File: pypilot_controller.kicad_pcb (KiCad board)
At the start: 4 copper layers, 76.6 x 50.6 mm, 82 parts, among them J1 power+, J2 power-, J3 power+, J4 power+, J5 UART_Device, J6 Rudder, J7 End Stops, J8 Conn_01x02, J9 ISP, Q1 Q_NMOS_GDS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

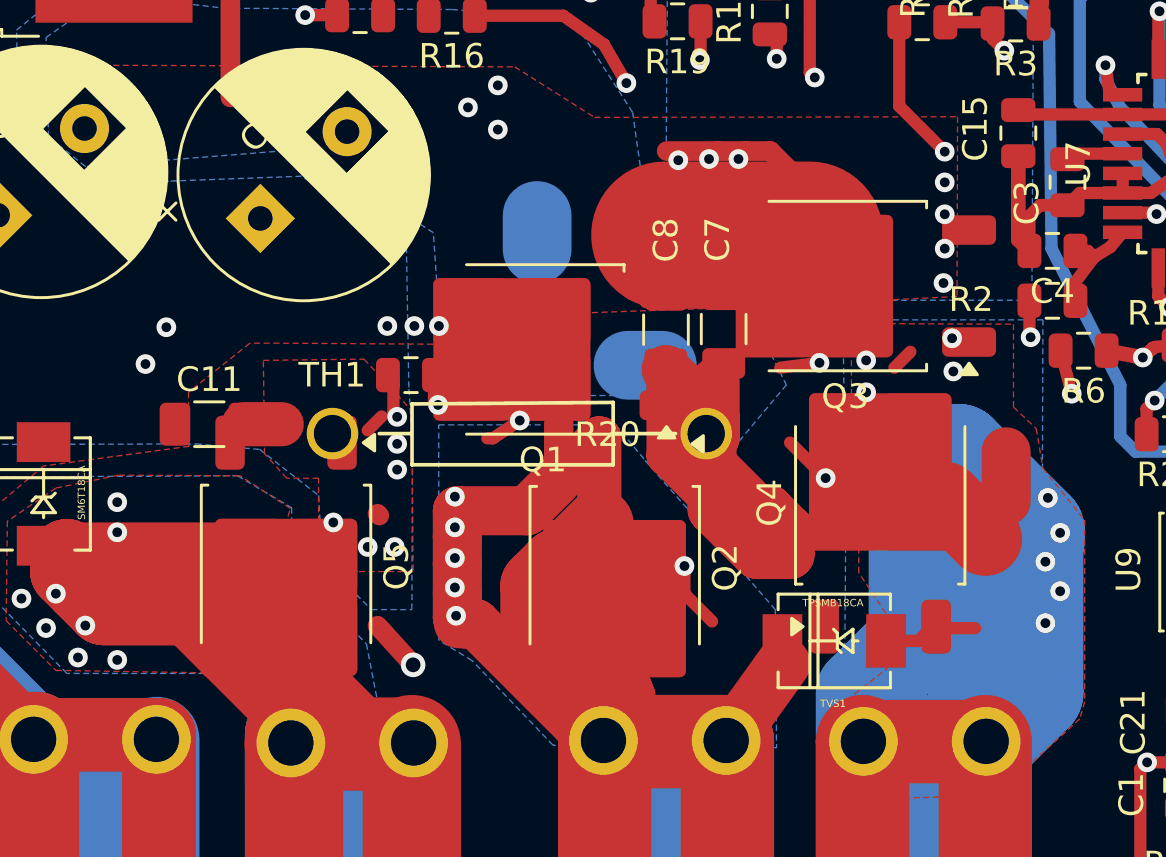
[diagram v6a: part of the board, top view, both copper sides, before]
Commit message: Shifted MOSFET locations to match original board
Centroid varies from original footprint
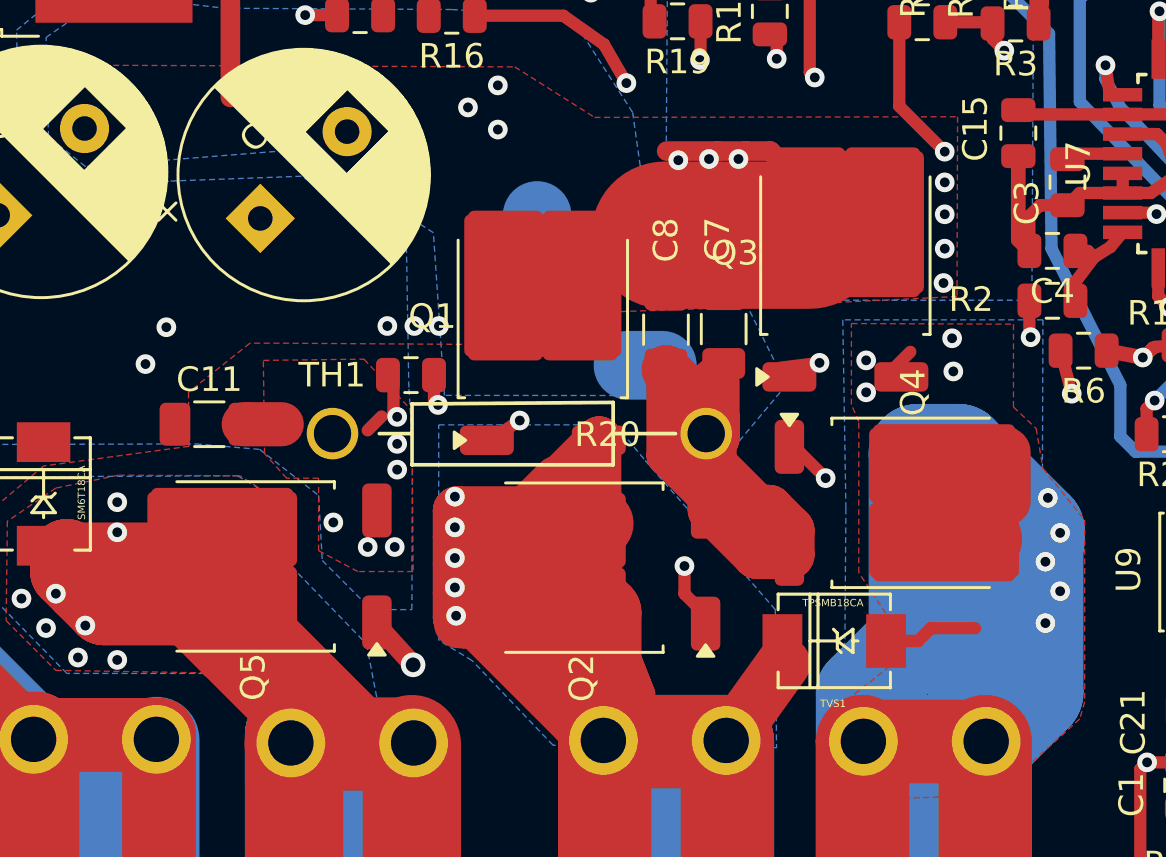
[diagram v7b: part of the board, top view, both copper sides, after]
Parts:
- moved Q1 1.34 mm to (32.2, 24.3), turned to 90 degrees
- moved Q3 1.34 mm to (44.5, 21.7), turned to 90 degrees
- moved Q2 1.34 mm to (33.8, 34.5), turned to 180 degrees
- moved Q4 1.34 mm to (47.3, 31.9), turned to 0 degrees
- moved Q5 1.34 mm to (20.4, 34.4), turned to 180 degrees
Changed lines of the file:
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@@
 	(footprint "Package_TO_SOT_SMD:TO-252-2"
 		(layer "F.Cu")
-		(at 45.9232 31.8516 90)
+		(at 47.263 31.8516)
 		(descr "TO-252/DPAK SMD package, http://www.infineon.com/cms/en/product/packages/PG-TO252/PG-TO252-3-1/")
 		(tags "DPAK TO-252 DPAK-3 TO-252-3 SOT-428")
@@
 	(footprint "Package_TO_SOT_SMD:TO-252-2"
 		(layer "F.Cu")
-		(at 35.1106 34.4922 -90)
+		(at 33.7708 34.4922 180)
 		(descr "TO-252/DPAK SMD package, http://www.infineon.com/cms/en/product/packages/PG-TO252/PG-TO252-3-1/")
 		(tags "DPAK TO-252 DPAK-3 TO-252-3 SOT-428")
@@
 	(footprint "Package_TO_SOT_SMD:TO-252-2"
 		(layer "F.Cu")
-		(at 21.7248 34.4414 -90)
+		(at 20.385 34.4414 180)
 		(descr "TO-252/DPAK SMD package, http://www.infineon.com/cms/en/product/packages/PG-TO252/PG-TO252-3-1/")
 		(tags "DPAK TO-252 DPAK-3 TO-252-3 SOT-428")
@@
 	(footprint "Package_TO_SOT_SMD:TO-252-2"
 		(layer "F.Cu")
-		(at 44.5018 23.023 180)
+		(at 44.5018 21.6832 90)
 		(descr "TO-252/DPAK SMD package, http://www.infineon.com/cms/en/product/packages/PG-TO252/PG-TO252-3-1/")
 		(tags "DPAK TO-252 DPAK-3 TO-252-3 SOT-428")
@@
 	(footprint "Package_TO_SOT_SMD:TO-252-2"
 		(layer "F.Cu")
-		(at 32.1818 25.6032 180)
+		(at 32.1818 24.2634 90)
 		(descr "TO-252/DPAK SMD package, http://www.infineon.com/cms/en/product/packages/PG-TO252/PG-TO252-3-1/")
 		(tags "DPAK TO-252 DPAK-3 TO-252-3 SOT-428")

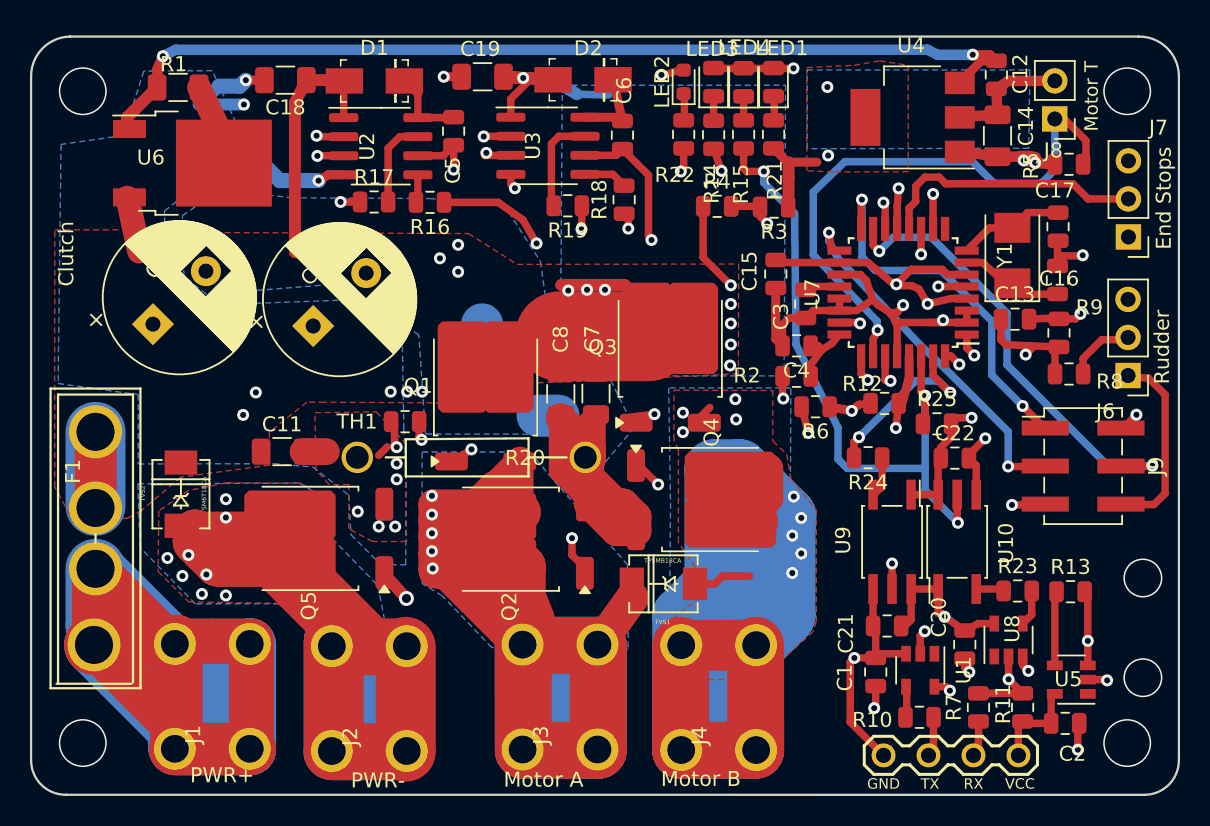
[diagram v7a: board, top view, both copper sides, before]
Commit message: Fixed MOSFET positions
New footprint has a different centroid
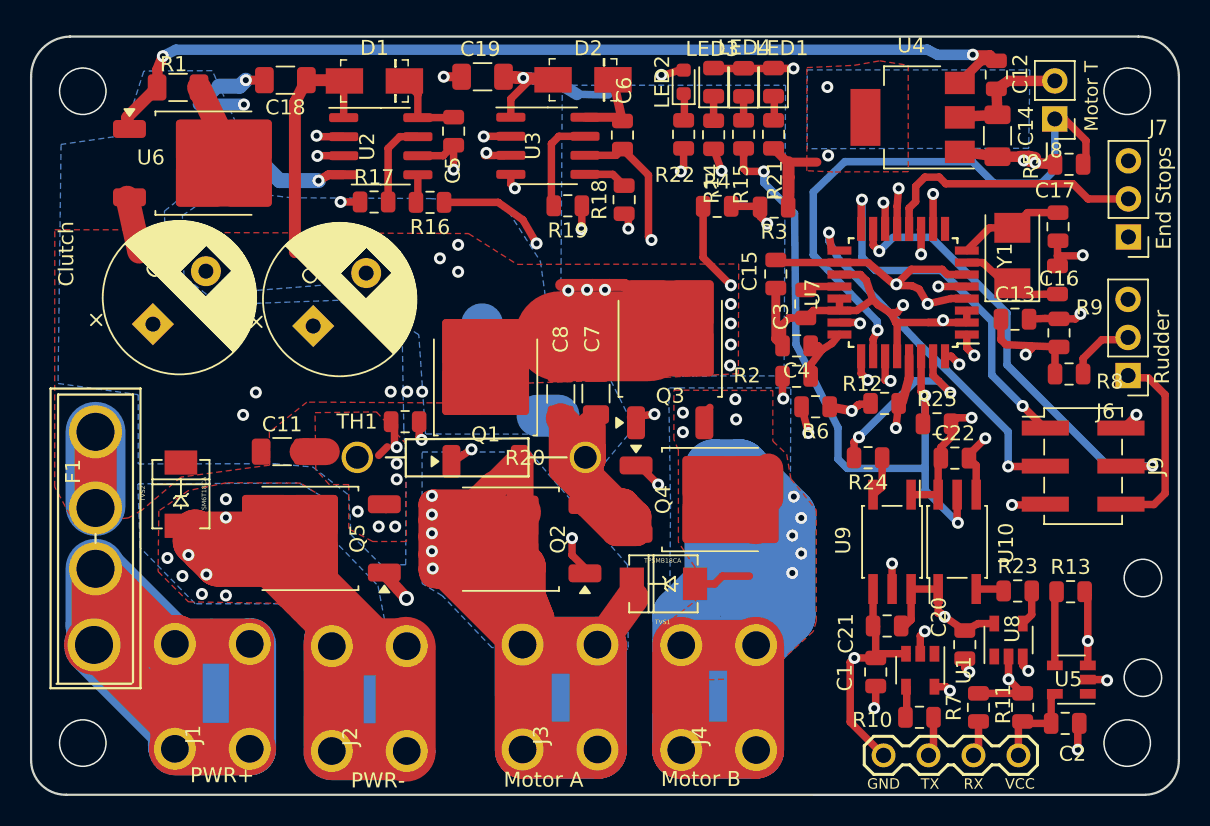
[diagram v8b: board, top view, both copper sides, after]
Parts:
- moved U6 1.34 mm to (13.5, 9.40)
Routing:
- net Net-(Q3-G): vias 3 -> 2
- net Net-(J4-Pin_1): vias 11 -> 10
- net Net-(J2-Pin_1): vias 9 -> 8
- net GND: vias 20 -> 21
- net +12V: vias 16 -> 18
